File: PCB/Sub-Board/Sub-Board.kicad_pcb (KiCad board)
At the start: 4 copper layers, 50.8 x 113 mm, 200 parts, among them J1 Conn_02x08, J10 Type, J11 Power/I2C, J12 Address, J13 Power/I2C, J14 Address, J15 GPIO, J16 Type, J17 GPIO, J18 Type, J19 Power/I2C, J2 Conn_01x04_Pin, J20 Address, J21 Power/I2C, J22 Address, J23 GPIO, J24 Type, J25 GPIO, J26 Type, J27 Power/I2C, J28 Address, J29 Power/I2C, J3 Power/I2C, J30 Address, J31 GPIO, J32 Type, J33 GPIO, J34 Type, J4 Address, J5 Power/I2C, J6 Address, J7 GPIO, J8 Type, J9 GPIO, SW1 SW_DIP_x07, U1 TPS629210DRLR, U2 74HC165, U3 STM32F401VETx, U4 74HC165, U5 74HC165, U6 74HC165, U7 74HC165, Y1 26 MHz

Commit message: Sub Board PCB: Parts Placement (wip)
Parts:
- J2: footprint Connector_PinHeader_2.54mm:PinHeader_1x04_P2.54mm_Vertical -> Connector_PinHeader_2.54mm:PinHeader_1x04_P2.54mm_Vertical_SMD_Pin1Right
- moved R100 139.7 mm to (103.1, 140.5), turned to -90 degrees
- moved R101 137.1 mm to (104.4, 140.5), turned to -90 degrees
- moved R102 134.5 mm to (105.7, 140.5), turned to -90 degrees
- moved R103 131.9 mm to (106.9, 140.5), turned to -90 degrees
- moved R126 130.8 mm to (128.5, 140.5), turned to -90 degrees
- moved R84 130.0 mm to (121.9, 144.0), turned to 180 degrees
- moved R127 128.1 mm to (129.8, 140.5), turned to -90 degrees
- moved R128 125.4 mm to (131.1, 140.5), turned to -90 degrees
- moved R85 125.2 mm to (121.9, 140.2), turned to 180 degrees
- moved R129 122.7 mm to (132.3, 140.5), turned to -90 degrees
- moved R96 121.5 mm to (122.9, 125.0), turned to 90 degrees
- moved R97 120.7 mm to (121.7, 125.0), turned to 90 degrees
- moved R98 119.9 mm to (120.4, 125.0), turned to 90 degrees
- moved R99 119.1 mm to (119.1, 125.0), turned to 90 degrees
- moved R111 118.7 mm to (147.3, 140.2), turned to 180 degrees
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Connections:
- D1 pad 2: /System Bus/SystemBus-Data -> /System Bus/SystemBus-Clock
- D1 pad 3: /System Bus/SystemBus-Clock -> /System Bus/SystemBus-Data
- R10 pad 1: /Board Address/BoardAddress2 -> /Board Address/BoardAddress4
- R11 pad 1: /Board Address/BoardAddress1 -> /Board Address/BoardAddress5
- R12 pad 1: /Board Address/BoardAddress0 -> /Board Address/BoardAddress6
- R6 pad 1: /Board Address/BoardAddress6 -> /Board Address/BoardAddress0
- R7 pad 1: /Board Address/BoardAddress5 -> /Board Address/BoardAddress1
- R8 pad 1: /Board Address/BoardAddress4 -> /Board Address/BoardAddress2
- SW1 pad 10: /Board Address/BoardAddress4 -> /Board Address/BoardAddress2
- SW1 pad 12: /Board Address/BoardAddress2 -> /Board Address/BoardAddress4
- SW1 pad 13: /Board Address/BoardAddress1 -> /Board Address/BoardAddress5
- SW1 pad 14: /Board Address/BoardAddress0 -> /Board Address/BoardAddress6
- SW1 pad 8: /Board Address/BoardAddress6 -> /Board Address/BoardAddress0
- SW1 pad 9: /Board Address/BoardAddress5 -> /Board Address/BoardAddress1
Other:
- board text added: "3.3V"
- board text added: "GND"
- board text added: "STM32 SWD"
- board text added: "SWCLK"
- board text added: "SWDIO"

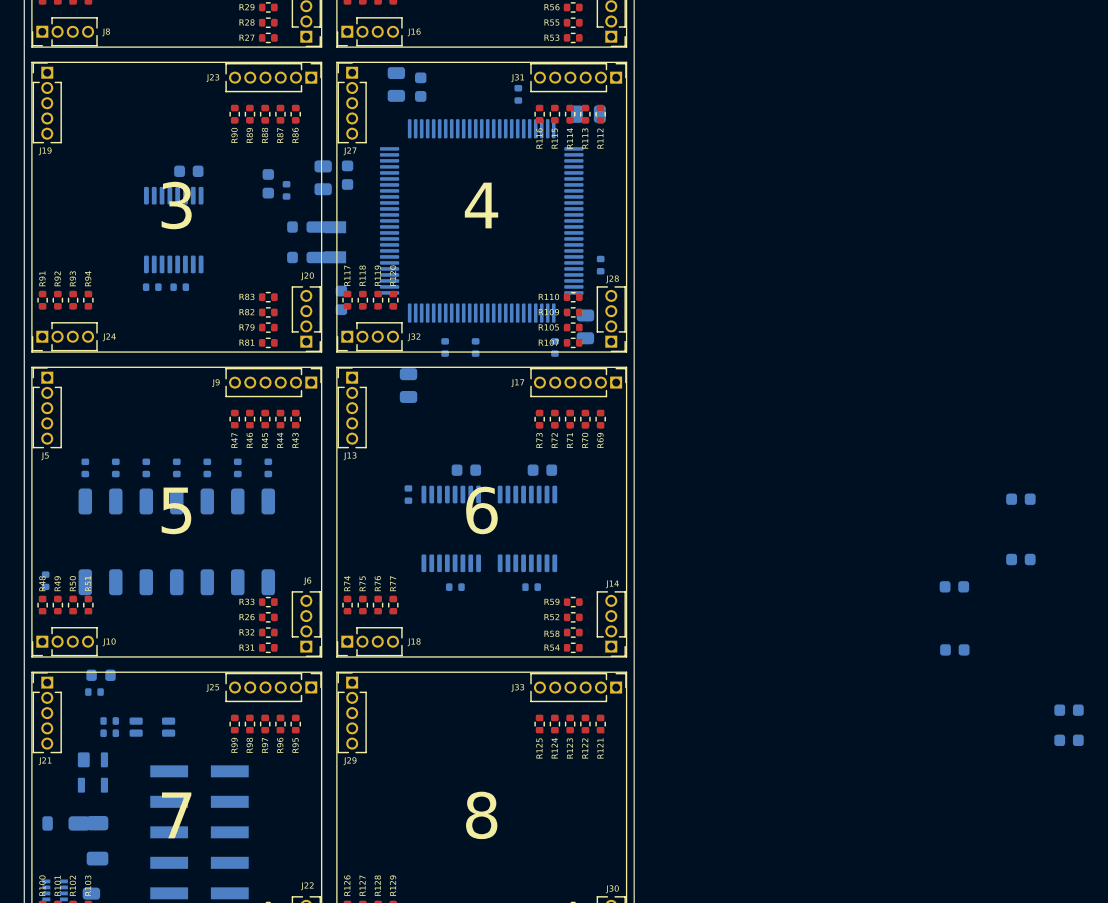
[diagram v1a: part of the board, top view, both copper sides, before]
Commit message: Sub Board PCB: Placement finished
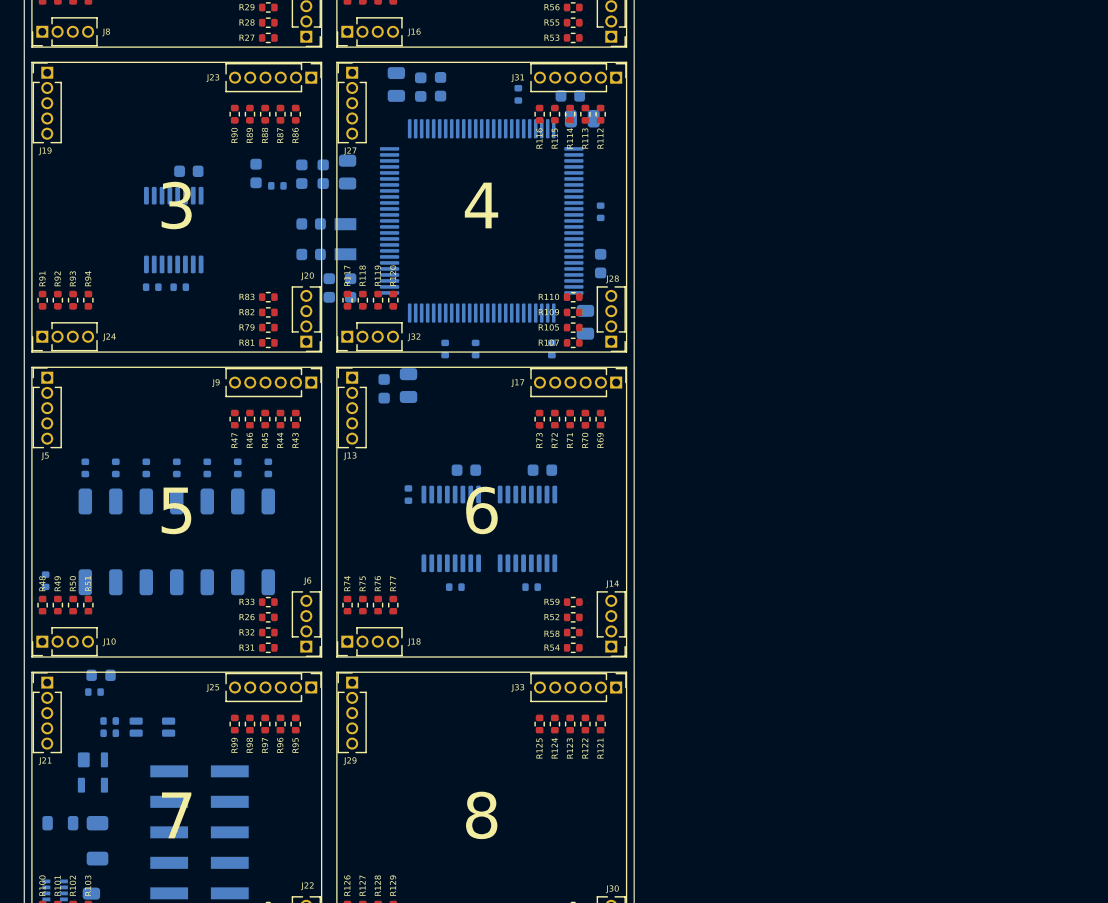
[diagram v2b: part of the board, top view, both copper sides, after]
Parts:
- moved C18 75.5 mm to (136.3, 71.9), turned to 90 degrees
- moved C12 68.0 mm to (124.7, 79.2), turned to 90 degrees
- moved C19 65.9 mm to (147.1, 72.6), turned to 180 degrees
- moved C15 60.2 mm to (127.0, 88.6), turned to -90 degrees
- moved C22 52.3 mm to (131.6, 97.0), turned to -90 degrees
- moved C11 39.9 mm to (149.6, 86.6), turned to 90 degrees
- moved R16 4.44 mm to (149.6, 82.3)
- moved C13 2.09 mm to (128.5, 79.0), turned to 90 degrees
- moved C16 2.03 mm to (126.5, 79.2), turned to 90 degrees
- moved C14 1.33 mm to (120.9, 79.1)
- moved C9 1.28 mm to (128.8, 88.6)
- moved Y1 0.88 mm to (128.4, 84.6)
- moved R23 0.85 mm to (122.7, 80.1), turned to 180 degrees
- moved C24 0.82 mm to (125.5, 83.3)
- moved C21 0.82 mm to (125.5, 85.9)
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
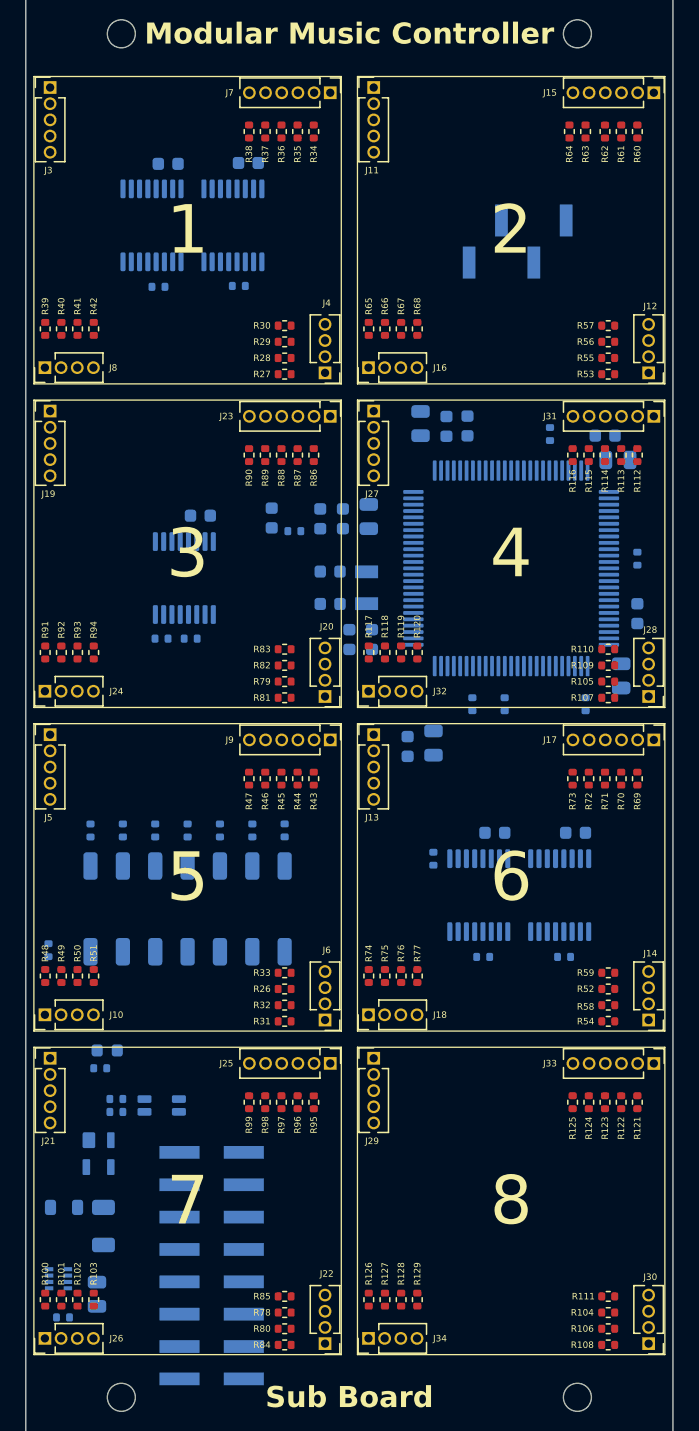
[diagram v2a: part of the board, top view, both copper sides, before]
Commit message: Sub Board PCB: Pin Connectors
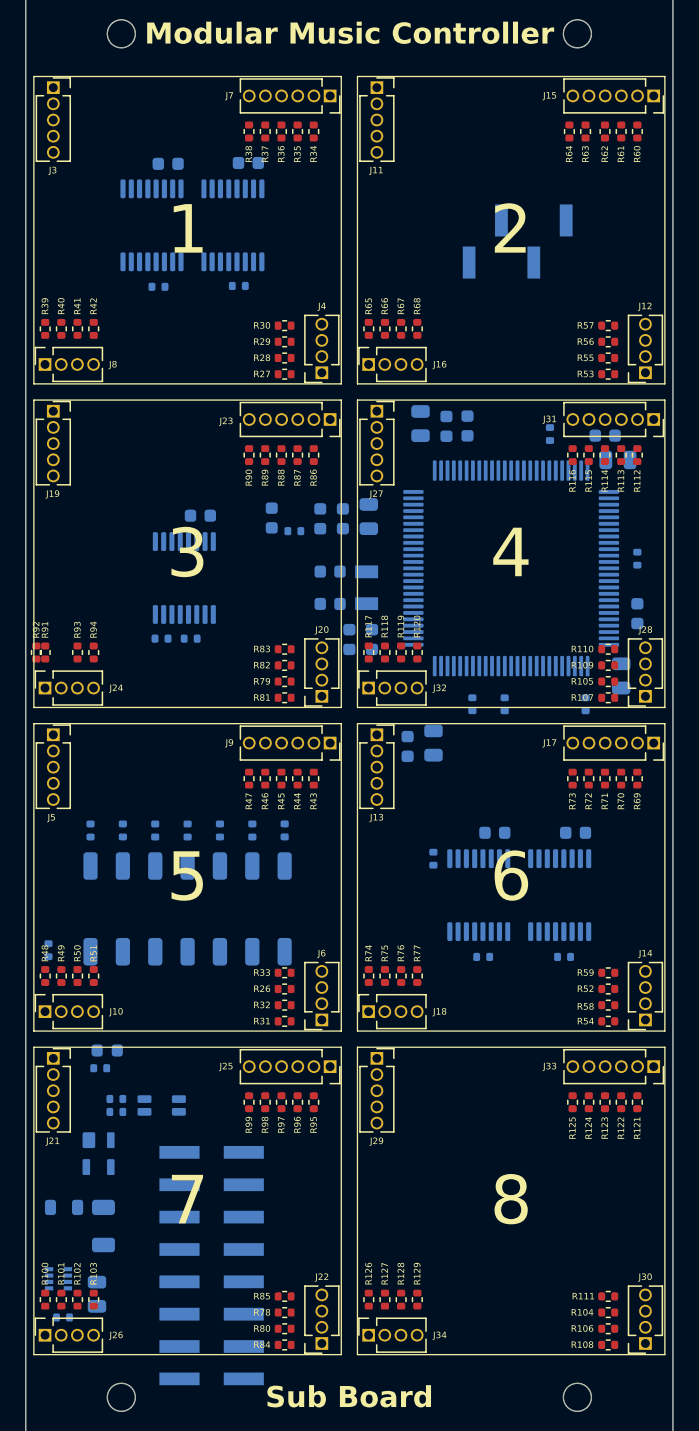
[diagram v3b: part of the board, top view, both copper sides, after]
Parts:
- J10, J12, J14, J16, J18, J20, J22, J24, J26, J28, J30, J32, J34, J4, J6, J8: footprint Connector_PinHeader_1.27mm:PinHeader_1x04_P1.27mm_Vertical -> Connector_PinSocket_1.27mm:PinSocket_1x04_P1.27mm_Vertical
- J11, J13, J19, J21, J27, J29, J3, J5: footprint Connector_PinHeader_1.27mm:PinHeader_1x05_P1.27mm_Vertical -> Connector_PinSocket_1.27mm:PinSocket_1x05_P1.27mm_Vertical
- J15, J17, J23, J25, J31, J33, J7, J9: footprint Connector_PinHeader_1.27mm:PinHeader_1x06_P1.27mm_Vertical -> Connector_PinSocket_1.27mm:PinSocket_1x06_P1.27mm_Vertical
- moved R92 1.96 mm to (102.4, 89.7)
- moved J25 0.26 mm to (125.5, 122.2)
- moved J15 0.25 mm to (150.9, 46.0)
- moved J17 0.25 mm to (150.9, 96.8)
- moved J31 0.25 mm to (150.9, 71.4)
- moved J33 0.25 mm to (150.9, 122.2)
- moved J10 0.25 mm to (103.1, 117.9)
- moved J11 0.25 mm to (129.2, 45.3)
- moved J12 0.25 mm to (150.2, 67.7)
- moved J13 0.25 mm to (129.2, 96.1)
- moved J14 0.25 mm to (150.2, 118.5)
- moved J21 0.25 mm to (103.8, 121.5)
- moved J23 0.25 mm to (125.5, 71.4)
- moved J24 0.25 mm to (103.1, 92.5)
- moved J26 0.25 mm to (103.1, 143.3)
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
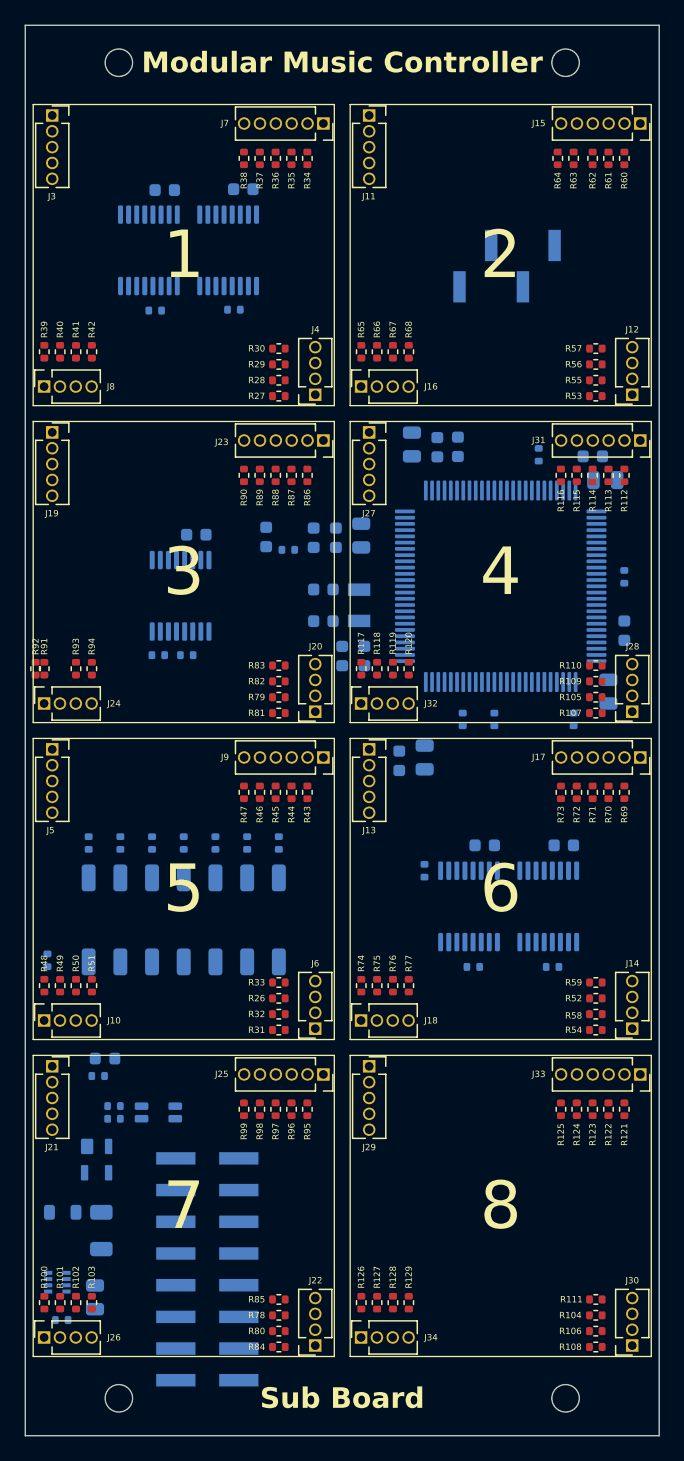
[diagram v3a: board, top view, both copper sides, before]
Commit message: Sub Board PCB: Board Setup
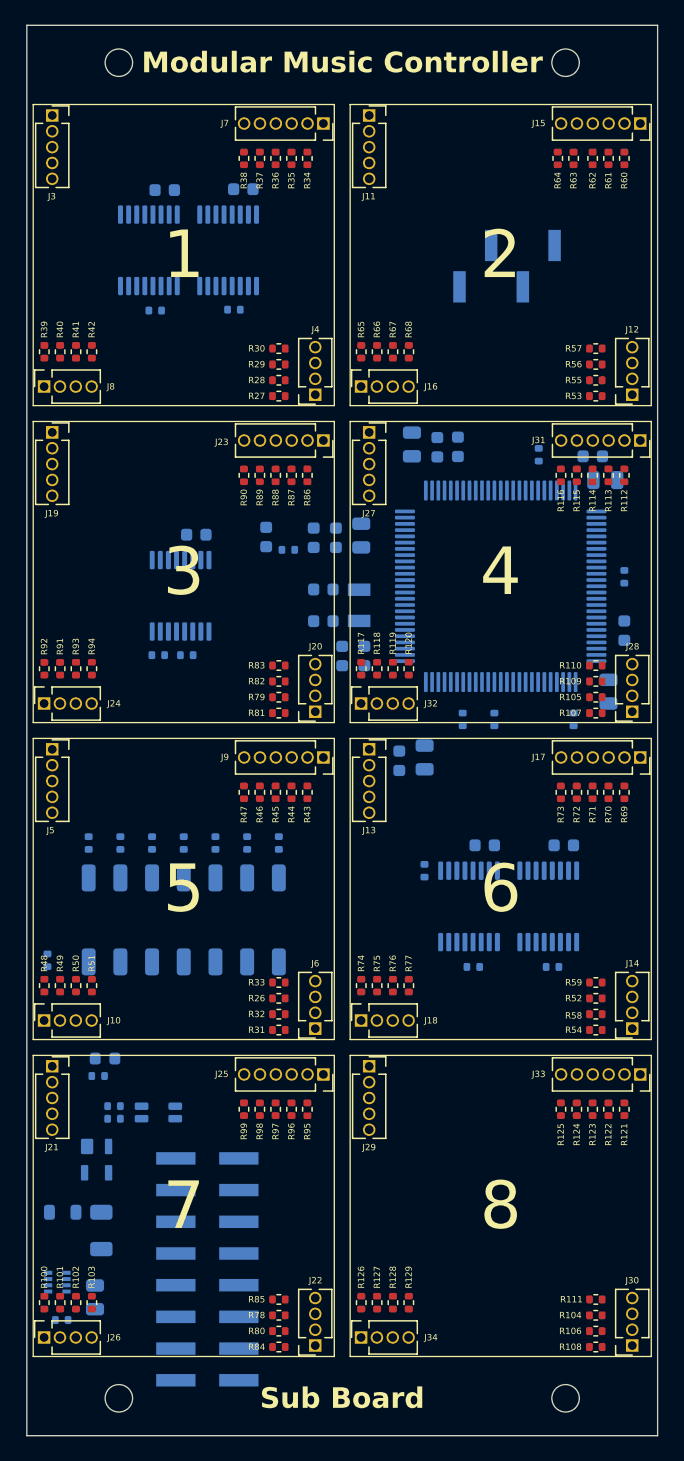
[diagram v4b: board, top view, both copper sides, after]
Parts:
- moved R91 1.27 mm to (104.4, 89.7)
- moved R92 0.69 mm to (103.1, 89.7)
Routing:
- added copper zone on In1.Cu, net /Board Address/+3.3V Digital
- added copper zone on In2.Cu, net GND
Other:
- board size 50.8 x 113 mm -> 50.5 x 113 mm
- board text removed: "TODO - Reduce with by 5 mil on each side at the very end"
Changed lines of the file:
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@@
 	(layers
 		(0 "F.Cu" signal)
-		(4 "In1.Cu" signal)
-		(6 "In2.Cu" signal)
+		(4 "In1.Cu" power)
+		(6 "In2.Cu" power)
 		(2 "B.Cu" signal)
 		(9 "F.Adhes" user "F.Adhesive")
@@
 	(footprint "Resistor_SMD:R_0402_1005Metric"
 		(layer "F.Cu")
-		(at 102.43 89.662 -90)
+		(at 103.124 89.664 -90)
 		(descr "Resistor SMD 0402 (1005 Metric), square (rectangular) end terminal, IPC-7351 nominal, (Body size source: IPC-SM-782 page 72, https://www.pcb-3d.com/wordpress/wp-content/uploads/ipc-sm-782a_amendment_1_and_2.pdf), generated with kicad-footprint-generator")
 		(tags "resistor")
@@
 	(footprint "Resistor_SMD:R_0402_1005Metric"
 		(layer "F.Cu")
-		(at 103.124 89.662 -90)
+		(at 104.394 89.664 -90)
 		(descr "Resistor SMD 0402 (1005 Metric), square (rectangular) end terminal, IPC-7351 nominal, (Body size source: IPC-SM-782 page 72, https://www.pcb-3d.com/wordpress/wp-content/uploads/ipc-sm-782a_amendment_1_and_2.pdf), generated with kicad-footprint-generator")
 		(tags "resistor")
@@
 	)
 	(gr_line
-		(start 101.6 151.13)
-		(end 101.6 38.1)
+		(start 101.727 151.13)
+		(end 101.727 38.1)
 		(stroke
 			(width 0.05)
 			(type default)
 		)
-		(locked yes)
 		(layer "Edge.Cuts")
 	)
 	(gr_line
-		(start 152.4 38.1)
-		(end 152.4 151.13)
+		(start 152.273 38.1)
+		(end 152.273 151.13)
 		(stroke
 			(width 0.05)
 			(type default)
 		)
-		(locked yes)
 		(layer "Edge.Cuts")
 	)
@@
 	)
 	(gr_line
-		(start 101.6 38.1)
-		(end 152.4 38.1)
+		(start 101.727 38.1)
+		(end 152.273 38.1)
 		(stroke
 			(width 0.05)
 			(type default)
 		)
-		(locked yes)
 		(layer "Edge.Cuts")
 	)
 	(gr_line
-		(start 152.4 151.13)
-		(end 101.6 151.13)
+		(start 152.273 151.13)
+		(end 101.727 151.13)
 		(stroke
 			(width 0.05)
 			(type default)
 		)
-		(locked yes)
 		(layer "Edge.Cuts")
 	)
@@
 		)
 	)
-	(gr_text "TODO - Reduce with by 5 mil on each side at the very end"
-		(at 101.6 36.83 0)
-		(layer "Cmts.User")
-		(effects
-			(font
-				(size 1 1)
-				(thickness 0.15)
+	(zone
+		(net 3)
+		(net_name "/Board Address/+3.3V Digital")
+		(layer "In1.Cu")
+		(name "3.3V Digital")
+		(hatch edge 0.5)
+		(connect_pads
+			(clearance 0.5)
+		)
+		(min_thickness 0.25)
+		(filled_areas_thickness no)
+		(fill yes
+			(thermal_gap 0.5)
+			(thermal_bridge_width 0.5)
+		)
+		(polygon
+			(pts
+				(xy 101.727 38.1) (xy 152.273 38.1) (xy 152.273 151.13) (xy 101.727 151.13)
+			)
+		)
+	)
+	(zone
+		(net 1)
+		(net_name "GND")
+		(layer "In2.Cu")
+		(name "GND")
+		(hatch edge 0.5)
+		(priority 1)
+		(connect_pads
+			(clearance 0.5)
+		)
+		(min_thickness 0.25)
+		(filled_areas_thickness no)
+		(fill yes
+			(thermal_gap 0.5)
+			(thermal_bridge_width 0.5)
+		)
+		(polygon
+			(pts
+				(xy 101.727 38.1) (xy 152.273 38.1) (xy 152.273 151.13) (xy 101.727 151.13)
 			)
-			(justify left bottom)
 		)
 	)
